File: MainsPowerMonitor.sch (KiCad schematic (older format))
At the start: 11 parts, among them J401 Screw_Terminal_01x02, J402 AudioJack2_SwitchT

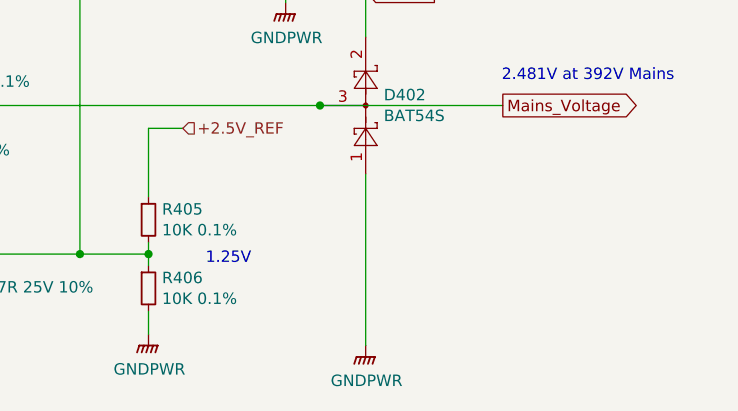
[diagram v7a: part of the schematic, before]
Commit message: Added a dedicated fuse for the charger connection.  Lowered the fuses from 25A to 20A after looking more closely at the data sheet.  Charger is 19.5A atmost and Battery current draw at 80% efficency, 86.8V, 1000W is 14.4A. Reduced the voltage divider resistance for the MainPowerMonitor from 2x 10K to 2x 1K, the reason for this is to draw 1.25mA from the 3.0V supply to increase its effectiveness as input protection for the micro inputs, the BAT54S diodes connect to the 3.0V power supplys so will conduct to this if the input risees a diode drop above 3.0V, so the more current draw from this supply the more it can sink without rising.
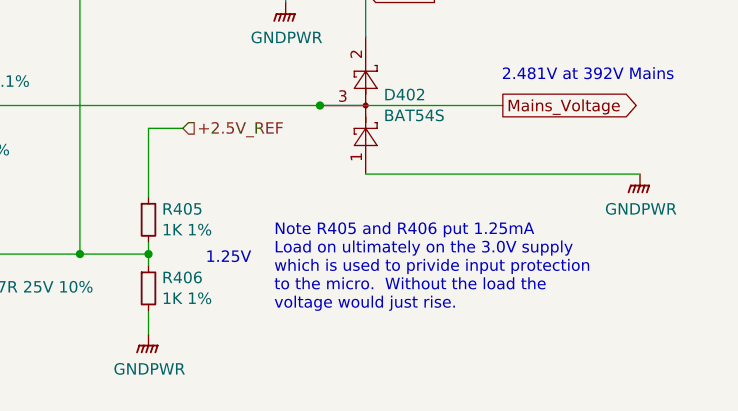
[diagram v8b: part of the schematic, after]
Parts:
- R405, R406: value 10K 0.1% -> 1K 1%; MFR Panasonic Electronic Components -> Yageo; MPN ERA-6AEB103V -> RC0805FR-071KL; SPN P10KDACT-ND -> 311-1.00KCRCT-ND
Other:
- note added: "Note R405 and R406 put 1.25mA\nLoad on ultimately on the 3.0V supply\nwhich is used to privide input protection\nto the micro. Without the load the \nvoltage would just rise."
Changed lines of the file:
@@
 P 4600 4450
 F 0 "R405" H 4659 4496 50  0000 L CNN
-F 1 "10K 0.1%" H 4659 4405 50  0000 L CNN
+F 1 "1K 1%" H 4659 4405 50  0000 L CNN
 F 2 "Resistor_SMD:R_0805_2012Metric_Pad1.15x1.40mm_HandSolder" H 4600 4450 50  0001 C CNN
-F 3 "https://industrial.panasonic.com/cdbs/www-data/pdf/RDM0000/AOA0000C307.pdf" H 4600 4450 50  0001 C CNN
-F 4 "Panasonic Electronic Components" H 0   0   50  0001 C CNN "MFR"
-F 5 "ERA-6AEB103V" H 0   0   50  0001 C CNN "MPN"
-F 6 "digikey" H 0   0   50  0001 C CNN "SPR"
-F 7 "P10KDACT-ND" H 0   0   50  0001 C CNN "SPN"
+F 3 "https://www.yageo.com/upload/media/product/productsearch/datasheet/rchip/PYu-RC_Group_51_RoHS_L_11.pdf" H 4600 4450 50  0001 C CNN
+F 4 "Yageo" H 0   0   50  0001 C CNN "MFR"
+F 5 "RC0805FR-071KL" H 0   0   50  0001 C CNN "MPN"
+F 6 "digikey" H 0   0   50  0001 C CNN "SPR"
+F 7 "311-1.00KCRCT-ND" H 0   0   50  0001 C CNN "SPN"
 F 8 "-" H 0   0   50  0001 C CNN "SPURL"
 	1    4600 4450
@@
 P 4600 4750
 F 0 "R406" H 4659 4796 50  0000 L CNN
-F 1 "10K 0.1%" H 4659 4705 50  0000 L CNN
+F 1 "1K 1%" H 4659 4705 50  0000 L CNN
 F 2 "Resistor_SMD:R_0805_2012Metric_Pad1.15x1.40mm_HandSolder" H 4600 4750 50  0001 C CNN
-F 3 "https://industrial.panasonic.com/cdbs/www-data/pdf/RDM0000/AOA0000C307.pdf" H 4600 4750 50  0001 C CNN
-F 4 "Panasonic Electronic Components" H 0   0   50  0001 C CNN "MFR"
-F 5 "ERA-6AEB103V" H 0   0   50  0001 C CNN "MPN"
-F 6 "digikey" H 0   0   50  0001 C CNN "SPR"
-F 7 "P10KDACT-ND" H 0   0   50  0001 C CNN "SPN"
+F 3 "https://www.yageo.com/upload/media/product/productsearch/datasheet/rchip/PYu-RC_Group_51_RoHS_L_11.pdf" H 4600 4750 50  0001 C CNN
+F 4 "Yageo" H 0   0   50  0001 C CNN "MFR"
+F 5 "RC0805FR-071KL" H 0   0   50  0001 C CNN "MPN"
+F 6 "digikey" H 0   0   50  0001 C CNN "SPR"
+F 7 "311-1.00KCRCT-ND" H 0   0   50  0001 C CNN "SPN"
 F 8 "-" H 0   0   50  0001 C CNN "SPURL"
 	1    4600 4750
@@
 L power:GNDPWR #PWR0404
 U 1 1 5F1789B6
-P 5550 5000
-F 0 "#PWR0404" H 5550 4800 50  0001 C CNN
-F 1 "GNDPWR" H 5554 4846 50  0000 C CNN
-F 2 "" H 5550 4950 50  0001 C CNN
-F 3 "" H 5550 4950 50  0001 C CNN
-	1    5550 5000
+P 6750 4250
+F 0 "#PWR0404" H 6750 4050 50  0001 C CNN
+F 1 "GNDPWR" H 6754 4096 50  0000 C CNN
+F 2 "" H 6750 4200 50  0001 C CNN
+F 3 "" H 6750 4200 50  0001 C CNN
+	1    6750 4250
 	1    0    0    -1
 $EndComp
@@
 Text Notes 1200 4650 0    50   ~ 0
 This transformer could be replaced with \nTi's isolated precision amplifier: AMC1100\nsee slaa552.pdf
+Text Label 1750 3900 0    50   ~ 0
+AC_Mains_Phase
+Text Label 1750 4000 0    50   ~ 0
+AC_Mains_Neutral
 Wire Wire Line
 	2500 3900 2400 3900
@@
 	3650 3950 3650 3900
 Wire Wire Line
-	5550 5000 5550 4250
+	6750 4250 5550 4250
 Wire Wire Line
 	5550 3650 5550 3450
@@
 Connection ~ 4300 3050
 Connection ~ 4300 2900
-Text Label 1750 3900 0    50   ~ 0
-AC_Mains_Phase
-Text Label 1750 4000 0    50   ~ 0
-AC_Mains_Neutral
+Text Notes 5150 4850 0    50   ~ 0
+Note R405 and R406 put 1.25mA\nLoad on ultimately on the 3.0V supply\nwhich is used to privide input protection\nto the micro.  Without the load the \nvoltage would just rise.
 $EndSCHEMATC
